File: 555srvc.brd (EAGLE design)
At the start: 34 x 27.9 mm, 11 parts, among them IC2 NE555P

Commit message: smd is go
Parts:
- added U$6: MOUNTINGHOLE2.0, microbuilder:MOUNTINGHOLE_2.0_PLATED
- C1: device SparkFun-Capacitors:AXIAL-5MM -> SparkFun-Capacitors:1206
- C2: device Panasonic-EE4:CAPPR500-1000X3200 -> Panasonic-EEE0_EEE1_EEE2_EEEFC:CAPAE1030X1050N
- D1: value 1N4004 -> (none); device adafruit:DO41-10 -> microbuilder:SOD-123
- IC2: value NE555P -> NE555D; device SparkFun-AnalogIC:DIL-08 -> SparkFun-AnalogIC:SO08
- R1, R2, R3, R4: device adafruit:0204/7 -> adafruit:R1206
- moved C2 26.1 mm to (6.73, 22.1), turned to 90 degrees
- moved D1 25.7 mm to (5.21, 11.9), turned to 270 degrees
- moved R2 23.9 mm to (10.2, 6.86), turned to 180 degrees
- moved R3 17.7 mm to (8.64, 12.1), turned to 270 degrees
- moved JP2 13.7 mm to (17.1, 22.1), turned to 90 degrees
- moved R1 11.1 mm to (16.3, 6.99), turned to 180 degrees
- moved C1 8.96 mm to (1.91, 11.9), turned to 270 degrees
- moved JP7 8.44 mm to (4.83, 1.78), turned to 180 degrees
- moved IC2 7.27 mm to (15.0, 11.9), turned to 90 degrees
- moved JP1 6.27 mm to (15.0, 1.78)
- moved R4 5.59 mm to (16.3, 17.0), turned to 0 degrees
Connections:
- net GND: now also C1.2; no longer C1.P$2
- net N$1: now also C1.1; no longer C1.P$1
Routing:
- net VCC: track 92.6 -> 0.00 mm
- net GND: track 59.7 -> 0.00 mm
- net N$1: track 31.8 -> 0.00 mm
- net N$2: track 14.0 -> 0.00 mm
- net N$5: track 5.08 -> 0.00 mm
- net N$4: track 3.81 -> 0.00 mm
- net SERVO_OUT: track 3.81 -> 0.00 mm
- net INPUT: track 3.81 -> 0.00 mm
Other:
- board size 34 x 27.9 mm -> 19.6 x 29.2 mm

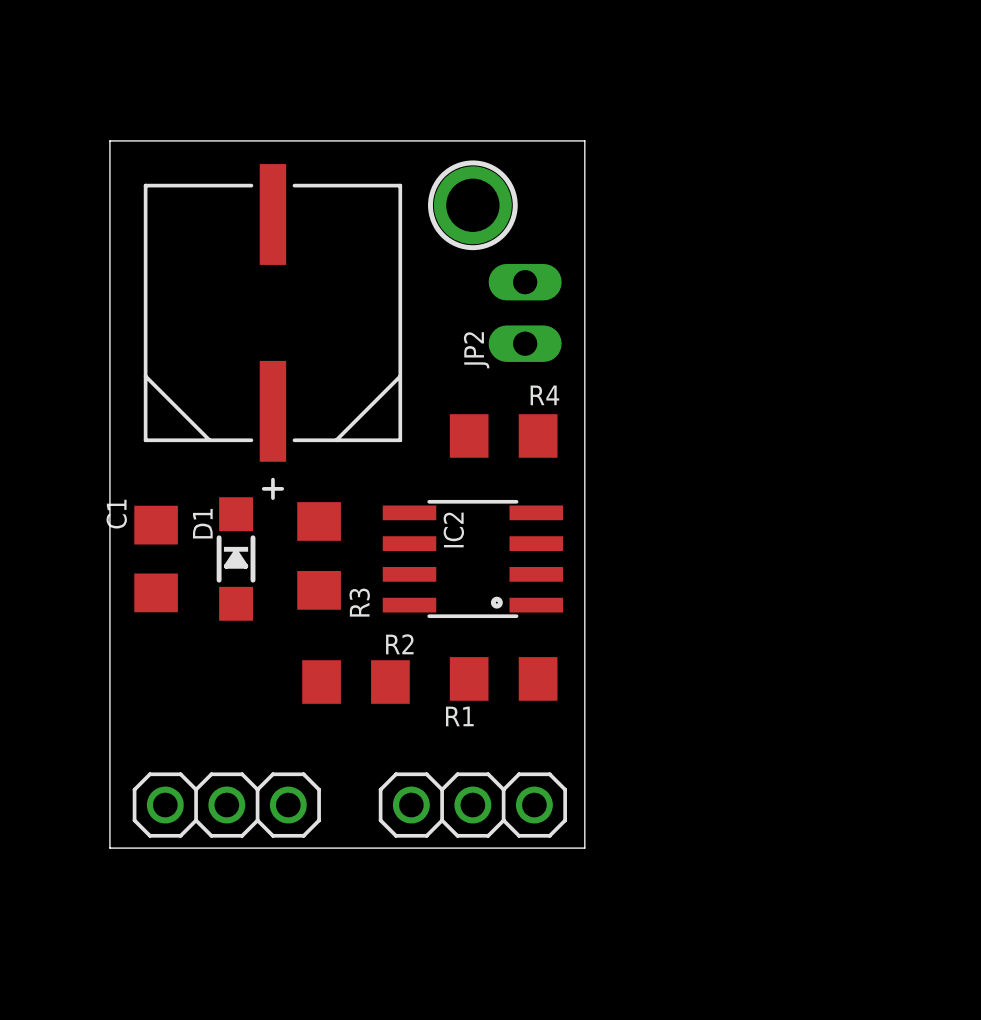
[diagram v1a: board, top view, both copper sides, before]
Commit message: crucial wiring change for standard servo wiring on JP1 and JP2
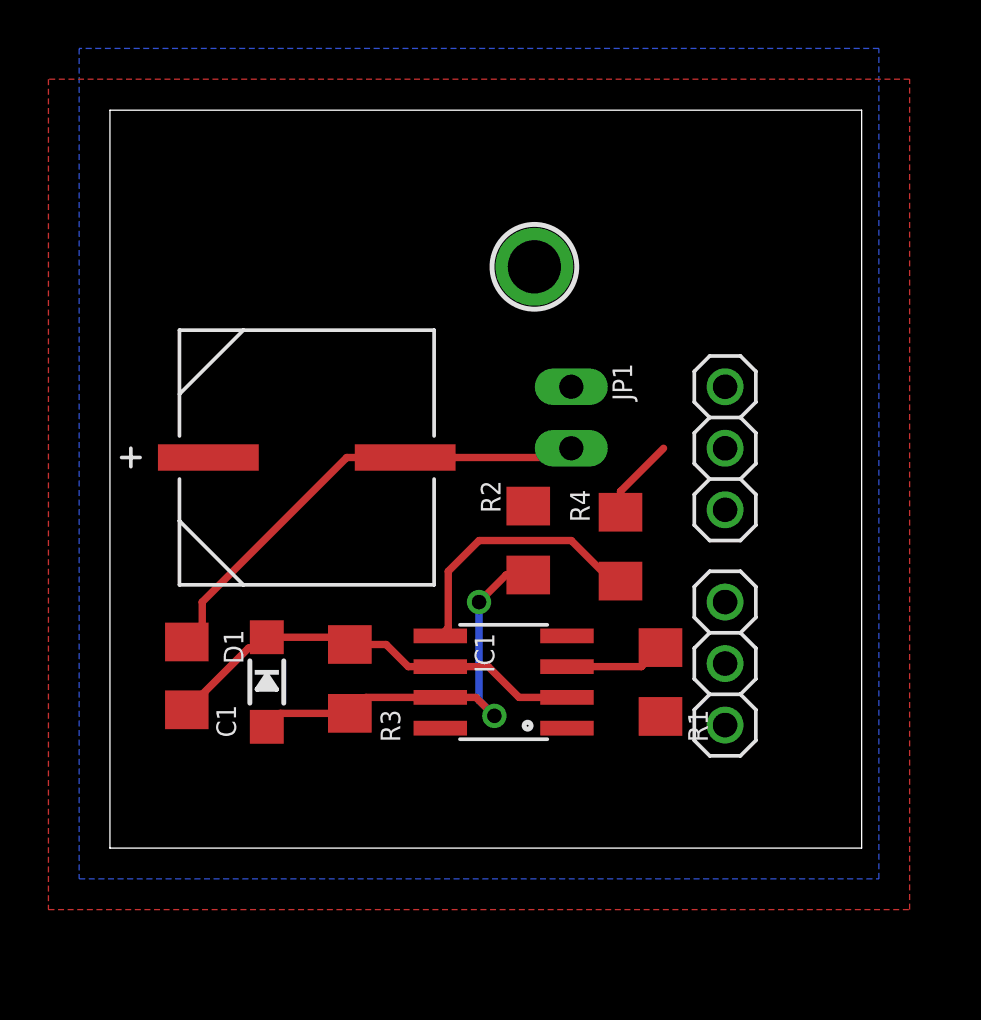
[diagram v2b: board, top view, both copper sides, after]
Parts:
- removed IC2: NE555D, SparkFun-AnalogIC:SO08
- removed JP7: SERVO_OUT, adafruit:1X03
- added IC1: NE555D, SparkFun-AnalogIC:SO08
- added JP3: INPUT / CV, adafruit:1X03
- JP1: value INPUT / CV -> 4.5-5.5V; device adafruit:1X03 -> microbuilder:1X02_OVAL
- JP2: value 4.5-5.5V -> SERVO_OUT; device microbuilder:1X02_OVAL -> adafruit:1X03
- moved JP2 16.7 mm to (25.4, 7.62), turned to 270 degrees
- moved JP1 16.5 mm to (19.1, 17.8), turned to 270 degrees
- moved R2 9.20 mm to (17.3, 12.7), turned to 270 degrees
- moved R4 6.65 mm to (21.1, 12.4), turned to 90 degrees
- moved R1 6.48 mm to (22.7, 6.86), turned to 270 degrees
- moved C2 6.13 mm to (8.13, 16.1), turned to 0 degrees
- moved D1 5.24 mm to (6.48, 6.86)
- moved R3 5.24 mm to (9.91, 6.99)
- moved C1 4.99 mm to (3.17, 7.11), turned to 90 degrees
- moved U$6 3.59 mm to (17.5, 24.0)
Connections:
- net GND: now also IC1.1, JP1.2, JP3.2; no longer IC2.1, JP1.3, JP7.3
- net INPUT: now also JP3.3; no longer JP1.2
- net N$1: now also IC1.2, IC1.6; no longer IC2.2, IC2.6
- net N$2: now also IC1.7; no longer IC2.7
- net N$4: now also IC1.5; no longer IC2.5
- net N$5: now also IC1.3; no longer IC2.3
- net SERVO_OUT: now also JP2.3; no longer JP7.2
- net VCC: now also IC1.4, IC1.8, JP3.1; no longer IC2.4, IC2.8, JP7.1
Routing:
- net GND: track 0.00 -> 21.5 mm
- net N$1: track 0.00 -> 18.0 mm
- net N$2: track 0.00 -> 17.7 mm, vias 0 -> 2
- net N$4: track 0.00 -> 11.1 mm
- net N$5: track 0.00 -> 4.19 mm
- net INPUT: track 0.00 -> 3.38 mm
- added copper zone on layer 16, net GND
- added copper zone on layer 1, net VCC
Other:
- board size 19.6 x 29.2 mm -> 31 x 30.5 mm

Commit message: smd added schema and board pdf,png
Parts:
- IC1: value NE555D -> 555
- JP1: device microbuilder:1X02_OVAL -> microbuilder:1X02_ROUND
- moved R2 17.1 mm to (3.05, 3.17)
- moved JP1 16.7 mm to (2.54, 15.2)
- moved U$6 7.69 mm to (20.4, 16.9)
- moved C2 3.59 mm to (10.7, 13.6)
- moved D1 3.43 mm to (6.60, 3.43)
- moved R1 3.01 mm to (21.3, 4.19)
- moved IC1 2.62 mm to (15.6, 4.32)
- moved JP3 2.54 mm to (25.4, 14.0)
- moved JP2 2.54 mm to (25.4, 5.08)
- moved R3 2.54 mm to (9.91, 4.45)
- moved C1 2.16 mm to (3.05, 9.27)
- moved R4 1.53 mm to (20.1, 11.3), turned to 0 degrees
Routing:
- net N$2: track 17.7 -> 10.5 mm, vias 2 -> 0
- net SERVO_OUT: track 0.00 -> 4.16 mm
- net N$4: track 11.1 -> 8.87 mm
- net GND: track 21.5 -> 23.7 mm
- net N$1: track 18.0 -> 17.3 mm
- net INPUT: track 3.38 -> 3.92 mm
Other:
- board size 31 x 30.5 mm -> 28.5 x 20.3 mm

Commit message: smd wip
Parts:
- removed JP1: 4.5-5.5V, microbuilder:1X02_ROUND
- removed U$6: MOUNTINGHOLE2.0, microbuilder:MOUNTINGHOLE_2.0_PLATED
- C1: device SparkFun-Capacitors:1206 -> ATtami:0805
- R1, R2, R3, R4: device adafruit:R1206 -> ATtami:0805
- moved JP2 24.0 mm to (1.40, 3.94), turned to 90 degrees
- moved R1 16.5 mm to (5.10, 1.32), turned to 180 degrees
- moved JP3 11.8 mm to (19.2, 3.94)
- moved R4 10.5 mm to (16.3, 1.52), turned to 270 degrees
- moved R2 10.3 mm to (12.8, 6.59), turned to 180 degrees
- moved R3 6.38 mm to (16.3, 5.08), turned to 90 degrees
- moved C1 6.24 mm to (6.24, 3.90)
- moved IC1 4.74 mm to (11.1, 2.90), turned to 270 degrees
- moved C2 4.33 mm to (10.4, 9.27), flipped to the bottom, turned to 180 degrees
- moved D1 2.72 mm to (4.44, 5.08), turned to 90 degrees
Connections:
- net GND: no longer JP1.2
- net VCC: no longer JP1.1
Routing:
- net VCC: track 0.00 -> 33.4 mm, vias 0 -> 1
- net N$2: track 10.5 -> 18.8 mm
- net N$4: track 8.87 -> 3.13 mm
- net N$1: track 17.3 -> 13.6 mm
- net GND: track 23.7 -> 20.0 mm, vias 0 -> 1
- net SERVO_OUT: track 4.16 -> 6.68 mm, vias 0 -> 1
- net N$5: track 4.03 -> 2.88 mm
- net INPUT: track 3.92 -> 4.47 mm
- removed copper zone on layer 16, net GND
- removed copper zone on layer 1, net VCC
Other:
- board size 28.5 x 20.3 mm -> 20.5 x 7.9 mm

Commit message: board layout
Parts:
- C2: value 1000UF -> (none); device Panasonic-EEE0_EEE1_EEE2_EEEFC:CAPAE1030X1050N -> adafruit:E5-6
- JP2, JP3: device adafruit:1X03 -> adafruit:1X03-CLEANBIG
- moved C2 7.90 mm to (4.70, 3.81), flipped to the top, turned to 90 degrees
- moved D1 6.90 mm to (11.2, 6.61), turned to 0 degrees
- moved R2 4.04 mm to (16.8, 5.94), turned to 270 degrees
- moved R1 3.23 mm to (3.05, 3.81), turned to 90 degrees
- moved R3 1.57 mm to (16.6, 3.56), turned to 180 degrees
- moved R4 0.40 mm to (16.6, 1.40), turned to 0 degrees
- moved C1 0.19 mm to (6.35, 4.06)
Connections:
- net GND: now also C2.-, JP3.1; no longer C2.2, JP3.2
- net VCC: now also C2.+, JP3.2; no longer C2.1, JP3.1
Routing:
- net N$2: track 18.8 -> 10.1 mm
- net SERVO_OUT: track 6.68 -> 2.52 mm, vias 1 -> 0
- net GND: track 20.0 -> 23.0 mm, vias 1 -> 0
- net VCC: track 33.4 -> 30.5 mm, vias 1 -> 0
- net N$1: track 13.6 -> 16.5 mm
- net INPUT: track 4.47 -> 1.64 mm
- net N$5: track 2.88 -> 5.70 mm
- net N$4: track 3.13 -> 2.19 mm

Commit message: added lib with all parts
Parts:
- C1, R1, R2, R3, R4: device ATtami:0805 -> 555srvc:0805
- C2: device adafruit:E5-6 -> 555srvc:E5-6
- D1: device microbuilder:SOD-123 -> 555srvc:SOD-123
- IC1: device SparkFun-AnalogIC:SO08 -> 555srvc:SO08
- JP2, JP3: device adafruit:1X03-CLEANBIG -> 555srvc:1X03-CLEANBIG
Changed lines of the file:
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@@
 </autorouter>
 <elements>
-<element name="C1" library="ATtami" package="0805" value="1uF" x="6.35" y="4.064" smashed="yes" rot="R90">
+<element name="C1" library="555srvc" package="0805" value="1uF" x="6.35" y="4.064" smashed="yes" rot="R90">
 <attribute name="NAME" x="7.128" y="4.493" size="0.8128" layer="25" rot="R180"/>
 <attribute name="VALUE" x="5.207" y="1.651" size="0.8128" layer="27" rot="R90"/>
 </element>
-<element name="D1" library="microbuilder" package="SOD-123" value="" x="11.176" y="6.605" smashed="yes">
+<element name="D1" library="555srvc" package="SOD-123" value="" x="11.176" y="6.605" smashed="yes">
 <attribute name="NAME" x="7.366" y="6.605" size="0.8128" layer="25" ratio="18"/>
 <attribute name="VALUE" x="9.906" y="4.827" size="0.4064" layer="27" ratio="10"/>
 </element>
-<element name="IC1" library="SparkFun-AnalogIC" package="SO08" value="555" x="11.096" y="2.905" smashed="yes" rot="R270">
+<element name="IC1" library="555srvc" package="SO08" value="555" x="11.096" y="2.905" smashed="yes" rot="R270">
 <attribute name="VALUE" x="11.985" y="-0.524" size="0.8128" layer="27"/>
 <attribute name="NAME" x="9.953" y="0.746" size="0.8128" layer="25"/>
 </element>
-<element name="JP3" library="adafruit" package="1X03-CLEANBIG" value="INPUT / CV" x="19.177" y="3.937" smashed="yes" rot="R270">
+<element name="JP3" library="555srvc" package="1X03-CLEANBIG" value="INPUT / CV" x="19.177" y="3.937" smashed="yes" rot="R270">
 <attribute name="VALUE" x="16.891" y="6.731" size="0.8128" layer="27" rot="R270"/>
 </element>
-<element name="JP2" library="adafruit" package="1X03-CLEANBIG" value="SERVO_OUT" x="1.397" y="3.937" smashed="yes" rot="R90">
+<element name="JP2" library="555srvc" package="1X03-CLEANBIG" value="SERVO_OUT" x="1.397" y="3.937" smashed="yes" rot="R90">
 <attribute name="VALUE" x="3.81" y="0.127" size="0.8128" layer="27" rot="R90"/>
 </element>
-<element name="R1" library="ATtami" package="0805" value="2.2k" x="3.048" y="3.81" smashed="yes" rot="R90">
+<element name="R1" library="555srvc" package="0805" value="2.2k" x="3.048" y="3.81" smashed="yes" rot="R90">
 <attribute name="NAME" x="3.81" y="4.191" size="0.8128" layer="25" rot="R180"/>
 <attribute name="VALUE" x="4.445" y="-1.016" size="0.8128" layer="27" rot="R90"/>
 </element>
-<element name="R2" library="ATtami" package="0805" value="1.5k" x="16.78" y="5.937" smashed="yes" rot="R270">
+<element name="R2" library="555srvc" package="0805" value="1.5k" x="16.78" y="5.937" smashed="yes" rot="R270">
 <attribute name="NAME" x="16.034" y="5.572" size="0.8128" layer="25"/>
 <attribute name="VALUE" x="15.002" y="5.429" size="0.8128" layer="27" rot="R270"/>
 </element>
-<element name="R3" library="ATtami" package="0805" value="47k" x="16.637" y="3.556" smashed="yes" rot="R180">
+<element name="R3" library="555srvc" package="0805" value="47k" x="16.637" y="3.556" smashed="yes" rot="R180">
 <attribute name="NAME" x="16.256" y="4.318" size="0.8128" layer="25" rot="R270"/>
 <attribute name="VALUE" x="19.685" y="5.588" size="0.8128" layer="27" rot="R180"/>
 </element>
-<element name="R4" library="ATtami" package="0805" value="15k" x="16.637" y="1.397" smashed="yes">
+<element name="R4" library="555srvc" package="0805" value="15k" x="16.637" y="1.397" smashed="yes">
 <attribute name="NAME" x="17.018" y="0.635" size="0.8128" layer="25" rot="R90"/>
 <attribute name="VALUE" x="13.97" y="2.413" size="0.8128" layer="27"/>
 </element>
-<element name="C2" library="adafruit" package="E5-6" value="" x="4.699" y="3.81" smashed="yes" rot="R90">
+<element name="C2" library="555srvc" package="E5-6" value="" x="4.699" y="3.81" smashed="yes" rot="R90">
 <attribute name="NAME" x="3.556" y="1.016" size="0.8128" layer="25" ratio="10" rot="R180"/>
 <attribute name="VALUE" x="7.62" y="6.858" size="1.27" layer="27" ratio="10" rot="R90"/>

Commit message: looks legit
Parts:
- moved R2 0.72 mm to (16.3, 5.43)
- moved D1 0.72 mm to (10.7, 6.10)
- moved IC1 0.72 mm to (10.6, 2.40)
- moved C1 0.72 mm to (5.84, 3.56)
- moved JP2 0.72 mm to (0.89, 3.43)
- moved R1 0.72 mm to (2.54, 3.30)
- moved JP3 0.72 mm to (18.7, 3.43)
- moved R3 0.72 mm to (16.1, 3.05)
- moved R4 0.72 mm to (16.1, 0.89)
- moved C2 0.64 mm to (4.19, 3.43)
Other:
- board size 20.5 x 7.9 mm -> 19.6 x 6.9 mm
- board text added: "1.9558/0.685 mm"

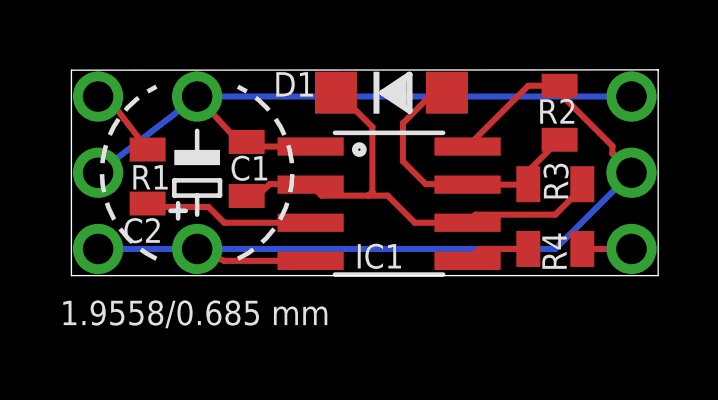
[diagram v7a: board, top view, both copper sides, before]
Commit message: changes pintout to coform with servo out.
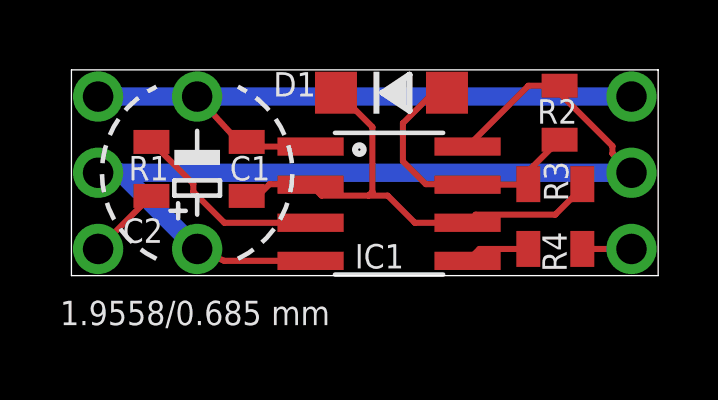
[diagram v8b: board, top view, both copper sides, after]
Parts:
- moved R1 0.28 mm to (2.67, 3.56), turned to 270 degrees
- turned JP2 to 270 degrees
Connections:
- net GND: now also JP2.1; no longer JP2.2
- net VCC: now also JP2.2; no longer JP2.1
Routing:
- net VCC: track 30.5 -> 33.8 mm
- net N$5: track 5.70 -> 6.58 mm
- net GND: track 23.2 -> 22.3 mm
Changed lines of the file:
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@@
 <wire x1="0" y1="0" x2="19.558" y2="0" width="0" layer="20"/>
 <wire x1="19.558" y1="0" x2="19.558" y2="6.858" width="0" layer="20"/>
-<wire x1="19.558" y1="6.858" x2="0" y2="6.848" width="0" layer="20"/>
-<wire x1="0" y1="6.848" x2="0" y2="0" width="0" layer="20"/>
+<wire x1="19.558" y1="6.858" x2="0" y2="6.858" width="0" layer="20"/>
+<wire x1="0" y1="6.858" x2="0" y2="0" width="0" layer="20"/>
 <text x="-0.381" y="-1.651" size="0.8128" layer="21">1.9558/0.685 mm</text>
 </plain>
@@
 <attribute name="VALUE" x="15.494" y="6.35" size="0.8128" layer="28" rot="MR270"/>
 </element>
-<element name="JP2" library="555srvc" package="1X03-CLEANBIG" value="SERVO_OUT" x="0.889" y="3.429" smashed="yes" rot="R90">
-<attribute name="VALUE" x="2.286" y="0" size="0.8128" layer="28" rot="MR90"/>
-</element>
-<element name="R1" library="555srvc" package="0805" value="2.2k" x="2.54" y="3.302" smashed="yes" rot="R90">
-<attribute name="NAME" x="3.302" y="3.683" size="0.8128" layer="25" rot="R180"/>
-<attribute name="VALUE" x="3.937" y="-1.524" size="0.8128" layer="27" rot="R90"/>
+<element name="JP2" library="555srvc" package="1X03-CLEANBIG" value="SERVO_OUT" x="0.889" y="3.429" smashed="yes" rot="R270">
+<attribute name="VALUE" x="-0.508" y="6.858" size="0.8128" layer="28" rot="MR270"/>
+</element>
+<element name="R1" library="555srvc" package="0805" value="2.2k" x="2.667" y="3.556" smashed="yes" rot="R270">
+<attribute name="NAME" x="1.905" y="3.175" size="0.8128" layer="25"/>
+<attribute name="VALUE" x="1.27" y="8.382" size="0.8128" layer="27" rot="R270"/>
 </element>
 <element name="R2" library="555srvc" package="0805" value="1.5k" x="16.272" y="5.429" smashed="yes" rot="R270">
@@
 <contactref element="IC1" pad="4"/>
 <contactref element="R2" pad="1"/>
-<contactref element="JP2" pad="1"/>
 <contactref element="C2" pad="+"/>
 <contactref element="JP3" pad="2"/>
-<wire x1="0.889" y1="0.889" x2="4.191" y2="0.889" width="0.2032" layer="16"/>
-<wire x1="4.191" y1="0.889" x2="16.129" y2="0.889" width="0.2032" layer="16"/>
-<wire x1="16.129" y1="0.889" x2="18.669" y2="3.429" width="0.2032" layer="16"/>
 <wire x1="7.9718" y1="0.492" x2="5.096" y2="0.492" width="0.2032" layer="1"/>
 <wire x1="5.096" y1="0.492" x2="4.191" y2="0.889" width="0.2032" layer="1"/>
@@
 <wire x1="18.034" y1="4.318" x2="18.034" y2="4.064" width="0.2032" layer="1"/>
 <wire x1="18.034" y1="4.064" x2="18.669" y2="3.429" width="0.2032" layer="1"/>
+<contactref element="JP2" pad="2"/>
+<wire x1="0.889" y1="3.429" x2="18.669" y2="3.429" width="0.6096" layer="16"/>
+<wire x1="0.889" y1="3.429" x2="1.651" y2="3.429" width="0.6096" layer="16"/>
+<wire x1="1.651" y1="3.429" x2="4.191" y2="0.889" width="0.6096" layer="16"/>
 </signal>
 <signal name="GND">
-<contactref element="JP2" pad="2"/>
 <contactref element="IC1" pad="1"/>
 <contactref element="C1" pad="2"/>
 <contactref element="C2" pad="-"/>
 <contactref element="JP3" pad="1"/>
-<wire x1="18.669" y1="5.969" x2="4.191" y2="5.969" width="0.2032" layer="16"/>
-<wire x1="4.191" y1="5.969" x2="0.889" y2="3.429" width="0.2032" layer="16"/>
+<wire x1="18.669" y1="5.969" x2="4.191" y2="5.969" width="0.6096" layer="16"/>
 <wire x1="7.9718" y1="4.302" x2="5.996" y2="4.302" width="0.2032" layer="1"/>
 <wire x1="5.996" y1="4.302" x2="5.842" y2="4.456" width="0.2032" layer="1"/>
 <wire x1="5.842" y1="4.456" x2="5.577" y2="4.456" width="0.2032" layer="1"/>
 <wire x1="5.577" y1="4.456" x2="4.191" y2="5.969" width="0.2032" layer="1"/>
+<contactref element="JP2" pad="1"/>
+<wire x1="4.191" y1="5.969" x2="0.889" y2="5.969" width="0.6096" layer="16"/>
 </signal>
 <signal name="N$1">
@@
 <contactref element="R1" pad="1"/>
 <wire x1="7.9718" y1="1.762" x2="5.096" y2="1.762" width="0.2032" layer="1"/>
-<wire x1="5.096" y1="1.762" x2="4.572" y2="2.286" width="0.2032" layer="1"/>
-<wire x1="4.572" y1="2.286" x2="2.656" y2="2.286" width="0.2032" layer="1"/>
-<wire x1="2.656" y1="2.286" x2="2.54" y2="2.402" width="0.2032" layer="1"/>
+<wire x1="5.096" y1="1.762" x2="4.064" y2="2.794" width="0.2032" layer="1"/>
+<wire x1="4.064" y1="2.794" x2="4.064" y2="3.059" width="0.2032" layer="1"/>
+<wire x1="4.064" y1="3.059" x2="2.667" y2="4.456" width="0.2032" layer="1"/>
 </signal>
 <signal name="SERVO_OUT">
 <contactref element="R1" pad="2"/>
 <contactref element="JP2" pad="3"/>
-<wire x1="0.889" y1="5.969" x2="1.185" y2="5.969" width="0.2032" layer="1"/>
-<wire x1="1.185" y1="5.969" x2="2.54" y2="4.202" width="0.2032" layer="1"/>
+<wire x1="2.667" y1="2.656" x2="2.656" y2="2.656" width="0.2032" layer="1"/>
+<wire x1="2.656" y1="2.656" x2="0.889" y2="0.889" width="0.2032" layer="1"/>
 </signal>
 <signal name="INPUT">
